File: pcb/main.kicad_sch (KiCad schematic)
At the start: 9 parts, among them IC1 DRV5032FB, J3 SJ-3541AS-SMT-TR-67

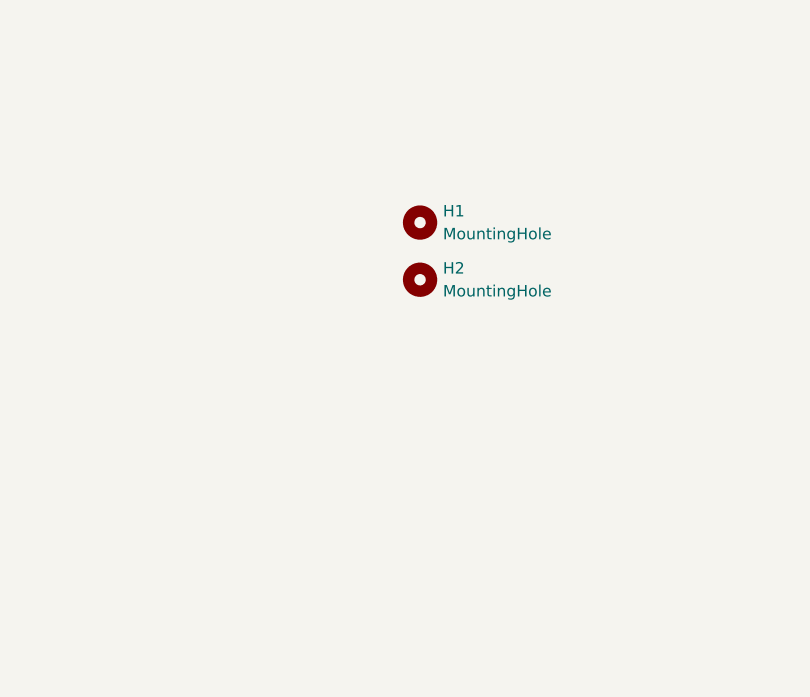
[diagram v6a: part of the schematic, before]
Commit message: Connected PCB GND with enclosure mounting screws
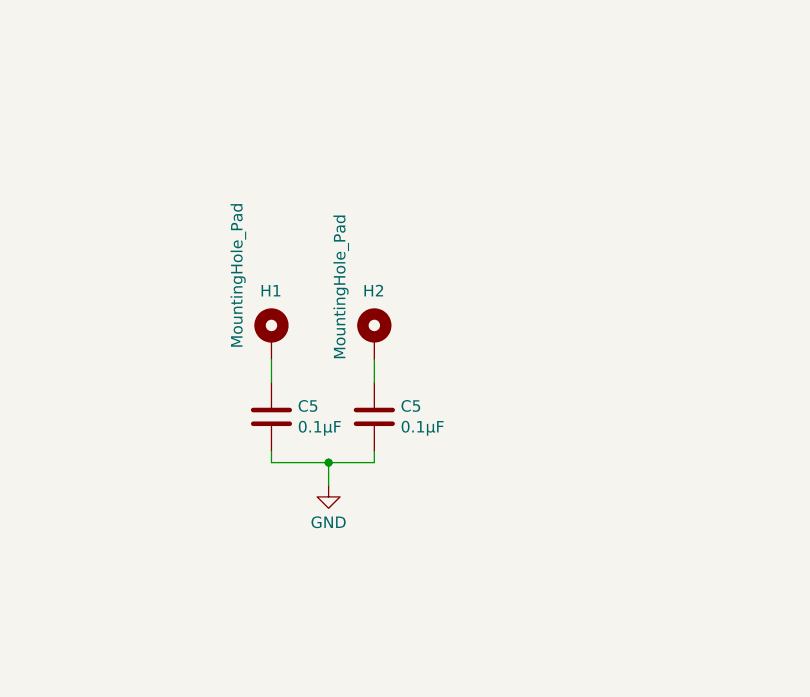
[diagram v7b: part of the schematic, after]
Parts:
- removed H1, H2: MountingHole, MountingHole:MountingHole_2.5mm_Pad, symbol Mechanical:MountingHole
- added C5 (x2): 0.1µF, Capacitor_SMD:C_0603_1608Metric, symbol Device:C
- added H1, H2: MountingHole_Pad, MountingHole:MountingHole_2.5mm_Pad_Via, symbol Mechanical:MountingHole_Pad
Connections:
- net GND: now also C5.2, C5.2
- new net: C5.1, H2.1
- new net: C5.1, H1.1
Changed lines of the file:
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@@
   (junction (at 254 109.22) (diameter 0) (color 0 0 0 0)
+  )
+  (junction (at 123.19 142.24) (diameter 0) (color 0 0 0 0)
   )
   (junction (at 52.07 154.94) (diameter 0) (color 0 0 0 0)
@@
     (stroke (width 0) (type default))
   )
+  (wire (pts (xy 128.27 130.81) (xy 128.27 133.35))
+    (stroke (width 0) (type default))
+  )
   (wire (pts (xy 125.73 39.37) (xy 143.51 39.37))
     (stroke (width 0) (type default))
@@
     (stroke (width 0) (type default))
   )
+  (wire (pts (xy 116.84 130.81) (xy 116.84 133.35))
+    (stroke (width 0) (type default))
+  )
   (wire (pts (xy 52.07 152.4) (xy 52.07 154.94))
     (stroke (width 0) (type default))
   )
+  (wire (pts (xy 128.27 142.24) (xy 123.19 142.24))
+    (stroke (width 0) (type default))
+  )
   (wire (pts (xy 251.46 111.76) (xy 254 111.76))
     (stroke (width 0) (type default))
@@
     (stroke (width 0) (type default))
   )
+  (wire (pts (xy 116.84 140.97) (xy 116.84 142.24))
+    (stroke (width 0) (type default))
+  )
+  (wire (pts (xy 123.19 142.24) (xy 123.19 144.78))
+    (stroke (width 0) (type default))
+  )
+  (wire (pts (xy 128.27 140.97) (xy 128.27 142.24))
+    (stroke (width 0) (type default))
+  )
   (wire (pts (xy 49.53 168.91) (xy 58.42 168.91))
     (stroke (width 0) (type default))
@@
   )
   (wire (pts (xy 57.15 38.1) (xy 87.63 38.1))
+    (stroke (width 0) (type default))
+  )
+  (wire (pts (xy 116.84 142.24) (xy 123.19 142.24))
     (stroke (width 0) (type default))
   )
@@
     (effects (font (size 1.27 1.27)) (justify left bottom))
   )
-  (symbol (lib_id "Mechanical:MountingHole") (at 133.35 121.92 0) (unit 1)
-    (in_bom no) (on_board yes) (dnp no) (fields_autoplaced)
-    (property "Reference" "H2" (at 135.89 120.65 0)
-      (effects (font (size 1.27 1.27)) (justify left))
-    )
-    (property "Value" "MountingHole" (at 135.89 123.19 0)
-      (effects (font (size 1.27 1.27)) (justify left))
-    )
-    (property "Footprint" "MountingHole:MountingHole_2.5mm_Pad" (at 133.35 121.92 0)
-      (effects (font (size 1.27 1.27)) hide)
-    )
-    (property "Datasheet" "~" (at 133.35 121.92 0)
-      (effects (font (size 1.27 1.27)) hide)
-    )
-    (instances
-      (project "rep-trap-pcb"
-        (path "/b363dc8f-4a45-4779-a397-ccb82393dab8/eebb1d37-a01d-4adf-be70-a8e8f9293475"
-          (reference "H2") (unit 1)
+  (symbol (lib_id "power:GND") (at 123.19 144.78 0) (unit 1)
+    (in_bom yes) (on_board yes) (dnp no) (fields_autoplaced)
+    (property "Reference" "#PWR074" (at 123.19 151.13 0)
+      (effects (font (size 1.27 1.27)) hide)
+    )
+    (property "Value" "GND" (at 123.19 148.9155 0)
+      (effects (font (size 1.27 1.27)))
+    )
+    (property "Footprint" "" (at 123.19 144.78 0)
+      (effects (font (size 1.27 1.27)) hide)
+    )
+    (property "Datasheet" "" (at 123.19 144.78 0)
+      (effects (font (size 1.27 1.27)) hide)
+    )
+    (pin "1")
+    (instances
+      (project "rep-trap-pcb"
+        (path "/b363dc8f-4a45-4779-a397-ccb82393dab8"
+          (reference "#PWR074") (unit 1)
+        )
+        (path "/b363dc8f-4a45-4779-a397-ccb82393dab8/eebb1d37-a01d-4adf-be70-a8e8f9293475"
+          (reference "#PWR01") (unit 1)
+        )
+      )
+    )
+  )
+  (symbol (lib_id "Device:C") (at 128.27 137.16 0) (unit 1)
+    (in_bom yes) (on_board yes) (dnp no)
+    (property "Reference" "C5" (at 131.191 135.9916 0)
+      (effects (font (size 1.27 1.27)) (justify left))
+    )
+    (property "Value" "0.1µF" (at 131.191 138.303 0)
+      (effects (font (size 1.27 1.27)) (justify left))
+    )
+    (property "Footprint" "Capacitor_SMD:C_0603_1608Metric" (at 129.2352 140.97 0)
+      (effects (font (size 1.27 1.27)) hide)
+    )
+    (property "Datasheet" "~" (at 128.27 137.16 0)
+      (effects (font (size 1.27 1.27)) hide)
+    )
+    (pin "1")
+    (pin "2")
+    (instances
+      (project "RP2040_minimal"
+        (path "/966e07a3-e14e-42ec-8301-447655da419c"
+          (reference "C5") (unit 1)
+        )
+      )
+      (project "rep-trap-pcb"
+        (path "/b363dc8f-4a45-4779-a397-ccb82393dab8/eebb1d37-a01d-4adf-be70-a8e8f9293475/e7ccec12-46ad-495a-887c-7169982423a2"
+          (reference "C15") (unit 1)
+        )
+        (path "/b363dc8f-4a45-4779-a397-ccb82393dab8/eebb1d37-a01d-4adf-be70-a8e8f9293475"
+          (reference "C19") (unit 1)
         )
       )
@@
     )
   )
+  (symbol (lib_id "Mechanical:MountingHole_Pad") (at 128.27 128.27 0) (unit 1)
+    (in_bom yes) (on_board yes) (dnp no)
+    (property "Reference" "H2" (at 127 123.19 0)
+      (effects (font (size 1.27 1.27)) (justify left))
+    )
+    (property "Value" "MountingHole_Pad" (at 124.46 130.81 90)
+      (effects (font (size 1.27 1.27)) (justify left))
+    )
+    (property "Footprint" "MountingHole:MountingHole_2.5mm_Pad_Via" (at 128.27 128.27 0)
+      (effects (font (size 1.27 1.27)) hide)
+    )
+    (property "Datasheet" "~" (at 128.27 128.27 0)
+      (effects (font (size 1.27 1.27)) hide)
+    )
+    (pin "1")
+    (instances
+      (project "rep-trap-pcb"
+        (path "/b363dc8f-4a45-4779-a397-ccb82393dab8/eebb1d37-a01d-4adf-be70-a8e8f9293475"
+          (reference "H2") (unit 1)
+        )
+      )
+    )
+  )
+  (symbol (lib_id "Device:C") (at 116.84 137.16 0) (unit 1)
+    (in_bom yes) (on_board yes) (dnp no)
+    (property "Reference" "C5" (at 119.761 135.9916 0)
+      (effects (font (size 1.27 1.27)) (justify left))
+    )
+    (property "Value" "0.1µF" (at 119.761 138.303 0)
+      (effects (font (size 1.27 1.27)) (justify left))
+    )
+    (property "Footprint" "Capacitor_SMD:C_0603_1608Metric" (at 117.8052 140.97 0)
+      (effects (font (size 1.27 1.27)) hide)
+    )
+    (property "Datasheet" "~" (at 116.84 137.16 0)
+      (effects (font (size 1.27 1.27)) hide)
+    )
+    (pin "1")
+    (pin "2")
+    (instances
+      (project "RP2040_minimal"
+        (path "/966e07a3-e14e-42ec-8301-447655da419c"
+          (reference "C5") (unit 1)
+        )
+      )
+      (project "rep-trap-pcb"
+        (path "/b363dc8f-4a45-4779-a397-ccb82393dab8/eebb1d37-a01d-4adf-be70-a8e8f9293475/e7ccec12-46ad-495a-887c-7169982423a2"
+          (reference "C15") (unit 1)
+        )
+        (path "/b363dc8f-4a45-4779-a397-ccb82393dab8/eebb1d37-a01d-4adf-be70-a8e8f9293475"
+          (reference "C20") (unit 1)
+        )
+      )
+    )
+  )
   (symbol (lib_id "power:GND") (at 217.17 148.59 0) (unit 1)
     (in_bom yes) (on_board yes) (dnp no) (fields_autoplaced)
@@
         (path "/b363dc8f-4a45-4779-a397-ccb82393dab8/eebb1d37-a01d-4adf-be70-a8e8f9293475"
           (reference "#PWR073") (unit 1)
+        )
+      )
+    )
+  )
+  (symbol (lib_id "Mechanical:MountingHole_Pad") (at 116.84 128.27 0) (unit 1)
+    (in_bom yes) (on_board yes) (dnp no)
+    (property "Reference" "H1" (at 115.57 123.19 0)
+      (effects (font (size 1.27 1.27)) (justify left))
+    )
+    (property "Value" "MountingHole_Pad" (at 113.03 129.54 90)
+      (effects (font (size 1.27 1.27)) (justify left))
+    )
+    (property "Footprint" "MountingHole:MountingHole_2.5mm_Pad_Via" (at 116.84 128.27 0)
+      (effects (font (size 1.27 1.27)) hide)
+    )
+    (property "Datasheet" "~" (at 116.84 128.27 0)
+      (effects (font (size 1.27 1.27)) hide)
+    )
+    (pin "1")
+    (instances
+      (project "rep-trap-pcb"
+        (path "/b363dc8f-4a45-4779-a397-ccb82393dab8/eebb1d37-a01d-4adf-be70-a8e8f9293475"
+          (reference "H1") (unit 1)
         )
       )
@@
         )
       )
-    )
-  )
-  (symbol (lib_id "Mechanical:MountingHole") (at 133.35 115.57 0) (unit 1)
-    (in_bom no) (on_board yes) (dnp no) (fields_autoplaced)
-    (property "Reference" "H1" (at 135.89 114.3 0)
-      (effects (font (size 1.27 1.27)) (justify left))
-    )
-    (property "Value" "MountingHole" (at 135.89 116.84 0)
-      (effects (font (size 1.27 1.27)) (justify left))
-    )
-    (property "Footprint" "MountingHole:MountingHole_2.5mm_Pad" (at 133.35 115.57 0)
-      (effects (font (size 1.27 1.27)) hide)
-    )
-    (property "Datasheet" "~" (at 133.35 115.57 0)
-      (effects (font (size 1.27 1.27)) hide)
-    )
-    (instances
-      (project "rep-trap-pcb"
-        (path "/b363dc8f-4a45-4779-a397-ccb82393dab8/eebb1d37-a01d-4adf-be70-a8e8f9293475"
-          (reference "H1") (unit 1)
-        )
-      )
